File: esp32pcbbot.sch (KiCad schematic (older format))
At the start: 9 parts, among them Q1 2N7002, Q2 2N7002, U2 CP2102N-A01-GQFN28, U3 ESP32-WROOM-32E

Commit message: esp32 swap for library compatibility
changed to esp32-waroom-32E to esp32-waroom-32. Maybe legacy lib?
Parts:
- removed U3: ESP32-WROOM-32E, Espressif:ESP32-WROOM-32E, symbol Espressif:ESP32-WROOM-32E
- added U1: ESP32-WROOM-32E-Espressif, Espressif:ESP32-WROOM-32E, symbol esp32pcbbot-rescue:ESP32-WROOM-32E-Espressif
- U2: symbol Interface_USB:CP2102N-A01-GQFN28 -> esp32pcbbot-rescue:CP2102N-A01-GQFN28-Interface_USB
- USB1: symbol Type-C:HRO-TYPE-C-31-M-12 -> esp32pcbbot-rescue:HRO-TYPE-C-31-M-12-Type-C
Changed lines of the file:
@@
 $EndDescr
 $Comp
-L Espressif:ESP32-WROOM-32E U3
-U 1 1 62575EEF
-P 7450 3900
-F 0 "U3" H 7475 5715 50  0000 C CNN
-F 1 "ESP32-WROOM-32E" H 7475 5624 50  0000 C CNN
-F 2 "Espressif:ESP32-WROOM-32E" H 7450 2150 50  0001 C CNN
-F 3 "https://www.espressif.com/sites/default/files/documentation/esp32-wroom-32e_esp32-wroom-32ue_datasheet_en.pdf" H 7850 3900 50  0001 C CNN
-	1    7450 3900
-	1    0    0    -1
-$EndComp
-$Comp
-L Interface_USB:CP2102N-A01-GQFN28 U2
+L esp32pcbbot-rescue:CP2102N-A01-GQFN28-Interface_USB U2
 U 1 1 62578773
 P 4100 3950
@@
 	5900 3350 6100 3350
 $Comp
-L Type-C:HRO-TYPE-C-31-M-12 USB1
+L esp32pcbbot-rescue:HRO-TYPE-C-31-M-12-Type-C USB1
 U 1 1 625B1879
 P 1650 3850
@@
 Wire Wire Line
 	5450 3250 6100 3250
+$Comp
+L esp32pcbbot-rescue:ESP32-WROOM-32E-Espressif U1
+U 1 1 625BF35E
+P 7450 3900
+F 0 "U1" H 7475 5715 50  0000 C CNN
+F 1 "ESP32-WROOM-32E-Espressif" H 7475 5624 50  0000 C CNN
+F 2 "Espressif:ESP32-WROOM-32E" H 7450 2150 50  0001 C CNN
+F 3 "" H 7850 3900 50  0001 C CNN
+	1    7450 3900
+	1    0    0    -1
+$EndComp
 $EndSCHEMATC

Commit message: added accellorometer
turnturn accellerate added BMI055
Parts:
- added IC?: BMI055, BMI055, symbol SamacSys_Parts:BMI055
- added S1: JS202011SCQN, JS202011SCQN, symbol SamacSys_Parts:JS202011SCQN
- added VR?: LM3940IMP-3.3_NOPB, VREG_LM3940IMP-3.3/NOPB, symbol LM3940IMP-3.3_NOPB:LM3940IMP-3.3_NOPB
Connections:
- net labels added: +3.3V, +3V3, +BATT, BATT_CHG, VBUS
- wire segments 60 -> 108
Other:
- note added: "(He Lives Within WIFI)"
- note added: "HAIL THURSDAY!\n"

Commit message: IO, Libload, and TODO
Added GPIO headers, fixed libload library and #todo list file.
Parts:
- added J?: SSQ-120-01-L-D, SSQ-120-XX-YYY-D, symbol SamacSys_Parts:SSQ-120-01-L-D
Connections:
- wire segments 108 -> 220
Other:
- moved on the sheet: IC?, U1

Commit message: added boot and en buttons, i2c pullup added, motor power switch added
modifications to make the design more general purpose.
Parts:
- added C? (x2): 0.1uF, symbol Device:C
- added R? (x2): 4.7k, symbol Device:R
- added S? (x2): TS-1187A-B-A-B, TS1187ABAB, symbol SamacSys_Parts:TS-1187A-B-A-B
- added S?: JS202011SCQN, JS202011SCQN, symbol SamacSys_Parts:JS202011SCQN
- added U?: L293D, Package_DIP:DIP-16_W7.62mm, symbol Driver_Motor:L293D
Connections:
- net labels added: BOOT, EN
- wire segments 220 -> 300

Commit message: generally finished the design
ayyy schematic is finished
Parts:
- added B1?: BATT_CHG_BOOST, ESP32bot:BATT_CHG_BOOST, symbol SamacSys_Parts:BATT_CHG_BOOST
- added C? (x6): EEEFC1V331P, EEEFK1V331P, symbol SamacSys_Parts:EEEFC1V331P
- added D1, D?: IRL81A, LED_THT:LED_SideEmitter_Rectangular_W4.5mm_H1.6mm, symbol LED:IRL81A
- added IC?: L78M05ABDT-TR, L78M05ABDTTR, symbol SamacSys_Parts:L78M05ABDT-TR
- added J?: 215299-4, RHDR4W78P0X254_1X4_1026X252X850P, symbol esp32pcbbot-rescue:215299-4-SamacSys_Parts
- added J? (x3): TB002-500-02BE, TB00250002BE, symbol SamacSys_Parts:TB002-500-02BE
- added Q? (x2): Q_Photo_NPN, symbol Device:Q_Photo_NPN
- added R? (x2): 100k, symbol Device:R
- added R? (x2): 300k, symbol Device:R
- added S?: DS01C-254-S-12BE, DS01C254S12BE, symbol SamacSys_Parts:DS01C-254-S-12BE
- added U?: 12BHC186P1-GR, 12BHC186P1GR, symbol SamacSys_Parts:12BHC186P1-GR
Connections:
- net labels added: 10A, 10Y, 11A, 11Y, 12A, 12Y, 7A, 7Y, 8A, 8Y, 9A, 9Y, M1A, M1B, M2A, M2B, VCC
- net labels removed: BATT_CHG
- wire segments 300 -> 459
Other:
- moved on the sheet: IC?, R?, S?, U?

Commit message: i made the pcb
horay i think its done
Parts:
- removed USB1: HRO-TYPE-C-31-M-12, symbol esp32pcbbot-rescue:HRO-TYPE-C-31-M-12-Type-C
- added J6: 215299-4, RHDR4W78P0X254_1X4_1026X252X850P, symbol esp32pcbbot-rescue:215299-4-SamacSys_Parts
- added USB1: TYPE-C-31-M-12, ESP32bot:USB_C_Receptacle_HRO_TYPE-C-31-M-12, symbol TYPE-C-31-M-12:TYPE-C-31-M-12
- C1, C2: renamed from C?; footprint (none) -> Capacitor_SMD:C_0603_1608Metric
- D1: footprint LED_THT:LED_SideEmitter_Rectangular_W4.5mm_H1.6mm -> LED_THT:LED_D3.0mm
- D2: renamed from D?; footprint LED_THT:LED_SideEmitter_Rectangular_W4.5mm_H1.6mm -> LED_THT:LED_D3.0mm
- Q3, Q4: renamed from Q?; footprint (none) -> SamacSys_Parts:QSD124A4R0
- R1, R2, R3, R4: footprint (none) -> Resistor_SMD:R_0603_1608Metric
- R10, R5, R6, R7, R8, R9: renamed from R?; footprint (none) -> Resistor_SMD:R_0603_1608Metric
- U1: footprint Espressif:ESP32-WROOM-32E -> SamacSys_Parts:ESP32WROOM32EM113EH3200PS3Q0
- VR1: renamed from VR?; footprint VREG_LM3940IMP-3.3/NOPB -> SamacSys_Parts:SOT230P700X180-4N
- gave numbers to parts that had none: 20
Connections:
- net +3V3: now also J6.4
- net 7Y: now also J6.2
- net 8Y: now also J6.3
- net GND: now also J6.1, USB1.A1 (GND), USB1.A12 (GND), USB1.B1 (GND), USB1.B12 (GND), USB1.S1 (SHIELD), USB1.S2 (SHIELD), USB1.S3 (SHIELD), USB1.S4 (SHIELD)
- net VBUS: now also USB1.A4 (VBUS), USB1.A9 (VBUS), USB1.B4 (VBUS), USB1.B9 (VBUS)
- net at U2.4 (D+): now also USB1.A6 (DP1), USB1.B6 (DP2)
- net at U2.5 (D-): now also USB1.A7 (DN1), USB1.B7 (DN2)
- net at R2.1: now also USB1.B5 (CC2)
- net at R1.1: now also USB1.A5 (CC1)
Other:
- moved on the sheet: J3

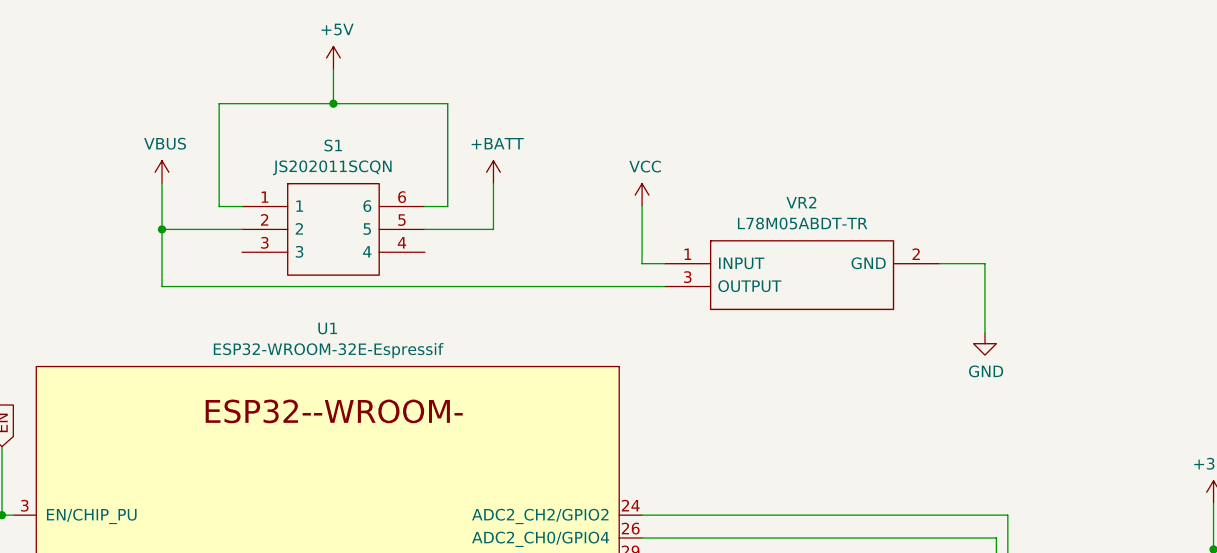
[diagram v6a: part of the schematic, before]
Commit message: ...and i sized a voltage regulator incorrectly
...goshdangit here we go again autorouting...
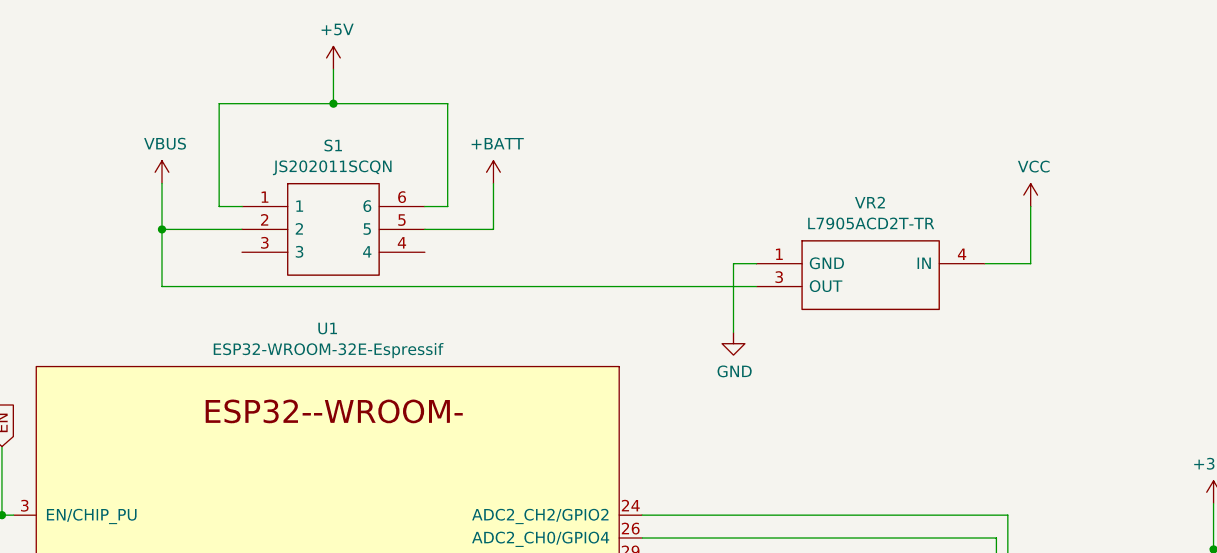
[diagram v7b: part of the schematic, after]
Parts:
- removed VR2: L78M05ABDT-TR, L78M05ABDTTR, symbol SamacSys_Parts:L78M05ABDT-TR
- added VR2: L7905ACD2T-TR, TO254P1542X460-3N, symbol SamacSys_Parts:L7905ACD2T-TR
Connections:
- net GND: now also VR2.1 (GND)
- net VBUS: now also VR2.3 (OUT)
- net VCC: now also VR2.4 (IN)
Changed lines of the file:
@@
 	14350 4300 14350 4700
-$Comp
-L SamacSys_Parts:L78M05ABDT-TR VR2
-U 1 1 64092ADF
-P 9200 1800
-F 0 "VR2" H 9800 2065 50  0000 C CNN
-F 1 "L78M05ABDT-TR" H 9800 1974 50  0000 C CNN
-F 2 "L78M05ABDTTR" H 10250 1900 50  0001 L CNN
-F 3 "https://datasheet.lcsc.com/szlcsc/STMicroelectronics-L78M05ABDT-TR_C58069.pdf" H 10250 1800 50  0001 L CNN
-F 4 "Linear Voltage Regulators 5.0V 0.5A Positive" H 10250 1700 50  0001 L CNN "Description"
-F 5 "2.4" H 10250 1600 50  0001 L CNN "Height"
-F 6 "STMicroelectronics" H 10250 1500 50  0001 L CNN "Manufacturer_Name"
-F 7 "L78M05ABDT-TR" H 10250 1400 50  0001 L CNN "Manufacturer_Part_Number"
-F 8 "511-L78M05ABDT-TR" H 10250 1300 50  0001 L CNN "Mouser Part Number"
-F 9 "https://www.mouser.co.uk/ProductDetail/STMicroelectronics/L78M05ABDT-TR?qs=kdoK93vJZIY3pGnUXsif4w%3D%3D" H 10250 1200 50  0001 L CNN "Mouser Price/Stock"
-F 10 "L78M05ABDT-TR" H 10250 1100 50  0001 L CNN "Arrow Part Number"
-F 11 "https://www.arrow.com/en/products/l78m05abdt-tr/stmicroelectronics?region=nac" H 10250 1000 50  0001 L CNN "Arrow Price/Stock"
-	1    9200 1800
-	1    0    0    -1
-$EndComp
 $Comp
 L power:VCC #PWR0134
@@
 Wire Wire Line
 	7000 1650 7000 1900
-Wire Wire Line
-	7000 1900 9200 1900
 $Comp
 L power:VCC #PWR0135
 U 1 1 628F37D4
-P 9100 1550
-F 0 "#PWR0135" H 9100 1400 50  0001 C CNN
-F 1 "VCC" H 9115 1723 50  0000 C CNN
-F 2 "" H 9100 1550 50  0001 C CNN
-F 3 "" H 9100 1550 50  0001 C CNN
-	1    9100 1550
-	1    0    0    -1
-$EndComp
-Wire Wire Line
-	9100 1550 9100 1800
-Wire Wire Line
-	9100 1800 9200 1800
+P 10800 1550
+F 0 "#PWR0135" H 10800 1400 50  0001 C CNN
+F 1 "VCC" H 10815 1723 50  0000 C CNN
+F 2 "" H 10800 1550 50  0001 C CNN
+F 3 "" H 10800 1550 50  0001 C CNN
+	1    10800 1550
+	1    0    0    -1
+$EndComp
 $Comp
 L power:GND #PWR0136
 U 1 1 62920831
-P 10600 2100
-F 0 "#PWR0136" H 10600 1850 50  0001 C CNN
-F 1 "GND" H 10605 1927 50  0000 C CNN
-F 2 "" H 10600 2100 50  0001 C CNN
-F 3 "" H 10600 2100 50  0001 C CNN
-	1    10600 2100
-	1    0    0    -1
-$EndComp
-Wire Wire Line
-	10400 1800 10600 1800
-Wire Wire Line
-	10600 1800 10600 2100
+P 9500 2100
+F 0 "#PWR0136" H 9500 1850 50  0001 C CNN
+F 1 "GND" H 9505 1927 50  0000 C CNN
+F 2 "" H 9500 2100 50  0001 C CNN
+F 3 "" H 9500 2100 50  0001 C CNN
+	1    9500 2100
+	1    0    0    -1
+$EndComp
+Wire Wire Line
+	9500 1800 9500 2100
 $Comp
 L power:GND #PWR0137
@@
 	1    0    0    -1
 $EndComp
+$Comp
+L SamacSys_Parts:L7905ACD2T-TR VR2
+U 1 1 628DC998
+P 9600 1800
+F 0 "VR2" H 10100 2065 50  0000 C CNN
+F 1 "L7905ACD2T-TR" H 10100 1974 50  0000 C CNN
+F 2 "TO254P1542X460-3N" H 10450 1900 50  0001 L CNN
+F 3 "http://www.st.com/web/en/resource/technical/document/datasheet/CD00000450.pdf" H 10450 1800 50  0001 L CNN
+F 4 "Voltage Regulator -5V 1.5A D2PAK L7905ACD2T-TR, Voltage Regulator, Negative 1.5A -5 V, +/-2%, 3-Pin D2PAK" H 10450 1700 50  0001 L CNN "Description"
+F 5 "4.6" H 10450 1600 50  0001 L CNN "Height"
+F 6 "511-L7905ACD2T-TR" H 10450 1500 50  0001 L CNN "Mouser Part Number"
+F 7 "https://www.mouser.co.uk/ProductDetail/STMicroelectronics/L7905ACD2T-TR?qs=22WmWNTp1rqzB5VVdeF8cw%3D%3D" H 10450 1400 50  0001 L CNN "Mouser Price/Stock"
+F 8 "STMicroelectronics" H 10450 1300 50  0001 L CNN "Manufacturer_Name"
+F 9 "L7905ACD2T-TR" H 10450 1200 50  0001 L CNN "Manufacturer_Part_Number"
+	1    9600 1800
+	1    0    0    -1
+$EndComp
+Wire Wire Line
+	9500 1800 9600 1800
+Wire Wire Line
+	10600 1800 10800 1800
+Wire Wire Line
+	10800 1800 10800 1550
+Wire Wire Line
+	7000 1900 9600 1900
 $EndSCHEMATC

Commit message: work pls work pls i beg u to finally work
the ground thingy has been updated
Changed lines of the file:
@@
 	11100 6250 10500 6250
 Wire Wire Line
-	13950 3500 13950 4050
+	13950 3500 13950 3900
 Connection ~ 13950 3500
 Wire Wire Line
@@
 Wire Wire Line
 	7000 1900 9600 1900
+$Comp
+L power:GNDPWR #PWR?
+U 1 1 628DA39C
+P 14400 4050
+F 0 "#PWR?" H 14400 3850 50  0001 C CNN
+F 1 "GNDPWR" H 14404 3896 50  0000 C CNN
+F 2 "" H 14400 4000 50  0001 C CNN
+F 3 "" H 14400 4000 50  0001 C CNN
+	1    14400 4050
+	1    0    0    -1
+$EndComp
+Wire Wire Line
+	14400 4050 14400 3900
+Wire Wire Line
+	14400 3900 13950 3900
+Connection ~ 13950 3900
+Wire Wire Line
+	13950 3900 13950 4050
 $EndSCHEMATC
